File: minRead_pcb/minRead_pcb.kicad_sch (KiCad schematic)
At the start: 0 parts

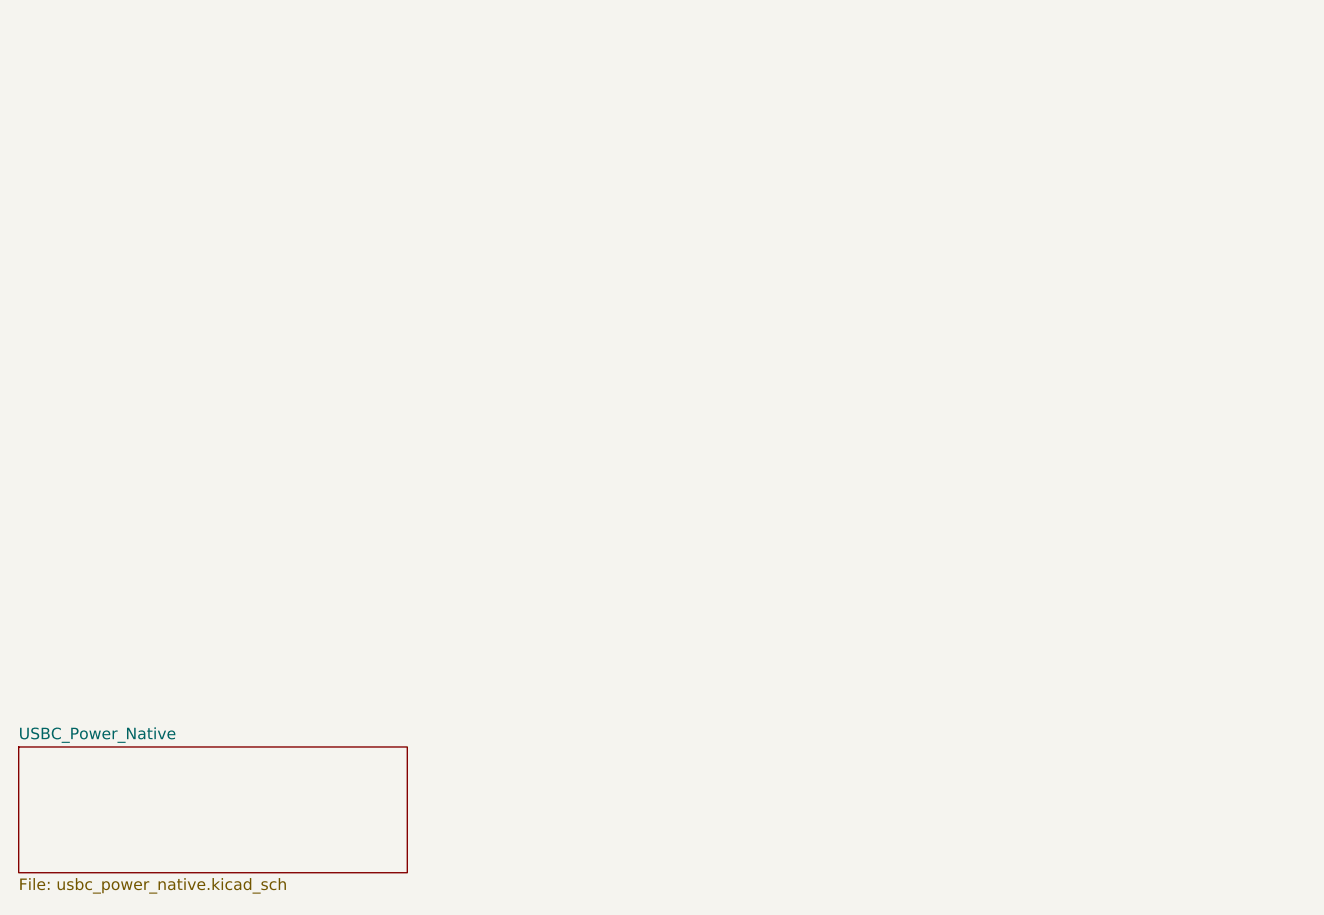
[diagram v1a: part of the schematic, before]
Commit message: - fixed diode orientation of eink booster - everything works except eink driver: - rst pin pulls high, dc doesn't toggle, etc etc. - TODO for next rev: - remove reset stabilizer and just route 3v3 to epd inductor circuit - replace esd arrays with hand-solderable components (qfn to sot) - replace buttons with resistor ladder circuit (xteink-like) - replace bq24074 with more discrete charging circuit to aid hand-solder - add led driver (15v to 7 series LEDs) - replace usb-c receptacle with through-hole - add external dupont pins for external LED driver access and spare GPIOs
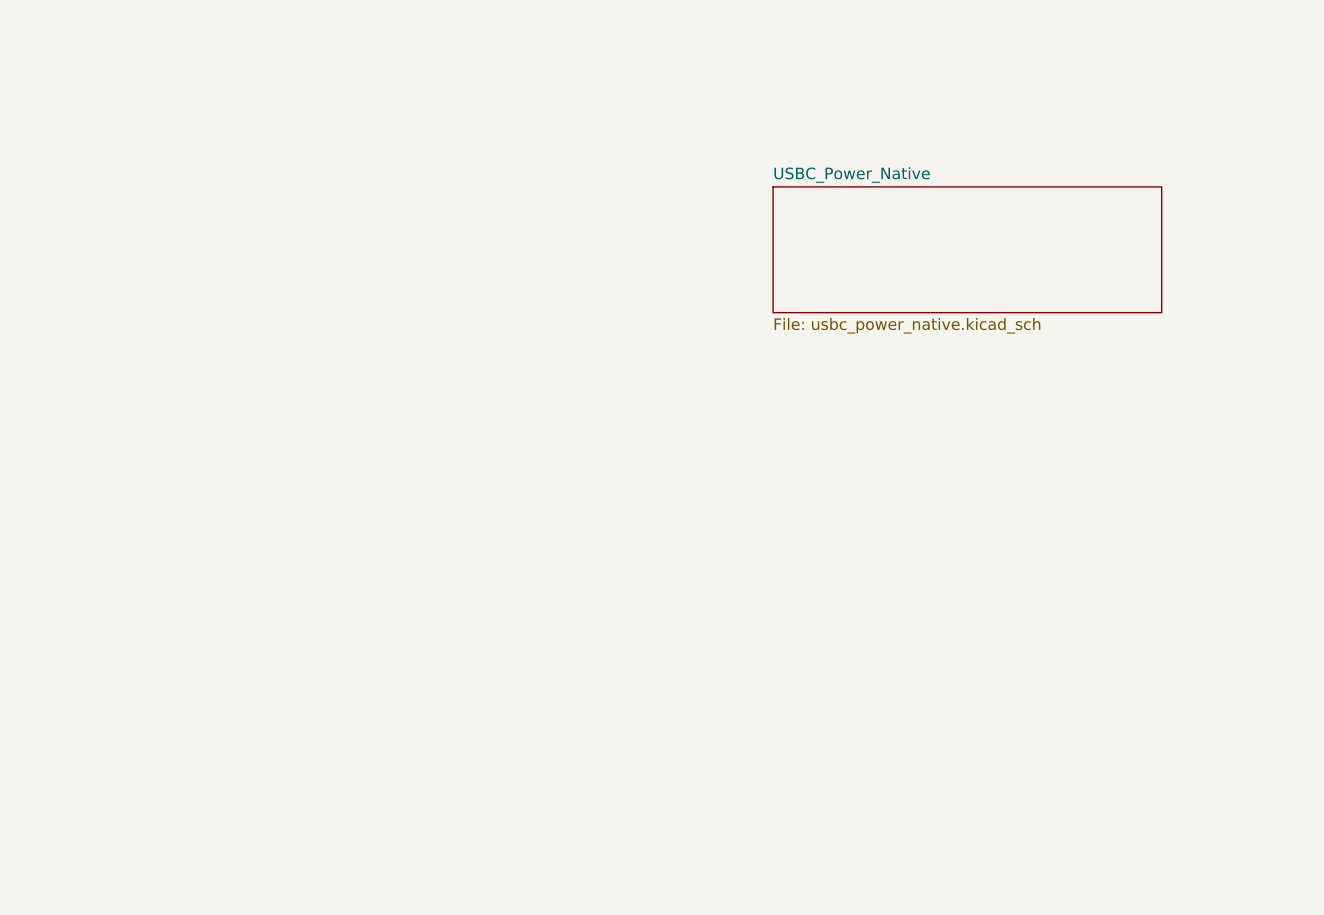
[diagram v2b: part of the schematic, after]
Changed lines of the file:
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@@
 	)
 	(sheet
-		(at 27.94 180.34)
+		(at 111.76 118.11)
 		(size 43.18 13.97)
 		(exclude_from_sim no)
@@
 		)
 		(property "Sheetname" "USBC_Power_Native"
-			(at 27.94 179.6284 0)
+			(at 111.76 117.3984 0)
 			(effects
 				(font
@@
 		)
 		(property "Sheetfile" "usbc_power_native.kicad_sch"
-			(at 27.94 194.8946 0)
+			(at 111.76 132.6646 0)
 			(effects
 				(font

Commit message: gigantic commit, my bad revised schematic to sanity check turns out my fpc was flipped, now fixed added following schematics: - battery protection circuit - series LED driver - external peripheral connector for unused GPIO revised following schematics: - power path, replaced with mcp charger and FET rather than bq - buttons, opted for resistor ladder circuit, added two more for xte compatibility - eink driver, opted to change to updated components from waveshare 2.3 - updated esd components for usb-c and sdmmc - updated usb-c receptacle, now through-hole
New layout:
- mostly same as last time, but work done to ensure good grounding for LED/eink circuits
- eink gpio has minimal crossing/coupling just in case
- esp32 and 24 pin headers have longer pads hopefully for easier soldering
- external header in corner back of device
- prettier passive component layout
- fat 3v3 traces and small zone fill

- todo:
- DRC errors, mostly clearance and silkscreen overlap
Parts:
- added C1: 1n, Capacitor_SMD:C_0805_2012Metric_Pad1.18x1.45mm_HandSolder, symbol Device:C
- added C10, C11, C12, C13, C14, C15, C16, C17, C2, C3, C37: 4.7u, Capacitor_SMD:C_0805_2012Metric_Pad1.18x1.45mm_HandSolder, symbol Device:C
- added C18, C19, C20, C22, C5, C9: 1u, Capacitor_SMD:C_0805_2012Metric_Pad1.18x1.45mm_HandSolder, symbol Device:C
- added C32, C4, C6: 22u, Capacitor_SMD:C_0805_2012Metric_Pad1.18x1.45mm_HandSolder, symbol Device:C
- added C33, C36, C7, C8: 0.1u, Capacitor_SMD:C_0805_2012Metric_Pad1.18x1.45mm_HandSolder, symbol Device:C
- added CR1: TSD05CDYFR, footprints:TVS_SOD2_DYF_TEX-M, symbol TSD05CDYFR:TSD05CDYFR
- added D1, D2, D3, D4, D5, D6: MBR0530, Diode_SMD:D_SOD-123, symbol Diode:MBR0530
- added H1, H2, H3, H4: MountingHole_Pad, MountingHole:MountingHole_2.2mm_M2_DIN965_Pad_TopBottom, symbol Mechanical:MountingHole_Pad
- added J1: USB_C_Receptacle, Connector_USB:USB_C_Receptacle_GCT_USB4085, symbol Connector:USB_C_Receptacle_USB2.0_14P
- added J2: FH34SRJ-24S-0.5SH_50_, FH34SRJ-24S-0.5SH(50):HRS_FH34SRJ-24S-0.5SH_50_, symbol FH34SRJ-24S-0.5SH(50):FH34SRJ-24S-0.5SH_50_
- added J3: FH34SRJ-6S-0.5SH_50_, FH34SRJ-6S-0.5SH(50):HRS_FH34SRJ-6S-0.5SH_50_, symbol FH34SRJ-6S-0.5SH(50):FH34SRJ-6S-0.5SH_50_
- added J4: PPTC062LFBN-RC, XPYC062LFBN-RC, symbol PPTC_12:PPTC062LFBN-RC
- added J5: Conn_01x02, Connector_JST:JST_PH_S2B-PH-K_1x02_P2.00mm_Horizontal, symbol Connector_Generic:Conn_01x02
- added J7: Micro_SD_Card, Connector_Card:microSD_HC_Hirose_DM3AT-SF-PEJM5, symbol Connector:Micro_SD_Card
- added L1, L2: 10u, srn3010C-100m:IND_SRN3010C-100M, symbol Device:L
- added Q1: FS8205A, Package_TO_SOT_SMD:SOT-23-6_Handsoldering, symbol FS8205A:FS8205A
- added Q2, Q3: IRLML6402, Package_TO_SOT_SMD:SOT-23_Handsoldering, symbol Transistor_FET:IRLML6402
- added Q4, Q5, Q6: BSS138, Package_TO_SOT_SMD:SOT-23, symbol Transistor_FET:BSS138
- added R1: 1M, Resistor_SMD:R_0805_2012Metric_Pad1.20x1.40mm_HandSolder, symbol Device:R
- added R10: 47k, Resistor_SMD:R_0805_2012Metric_Pad1.20x1.40mm_HandSolder, symbol Device:R
- added R11: 12k, Resistor_SMD:R_0805_2012Metric_Pad1.20x1.40mm_HandSolder, symbol Device:R
- added R12: 100k, Resistor_SMD:R_0805_2012Metric_Pad1.20x1.40mm_HandSolder, symbol Device:R
- added R13, R15, R28, R4, R53, R54, R55, R6, R7, R8, R9: 10k, Resistor_SMD:R_0805_2012Metric_Pad1.20x1.40mm_HandSolder, symbol Device:R
- added R14: 3, Resistor_SMD:R_0805_2012Metric_Pad1.20x1.40mm_HandSolder, symbol Device:R
- added R16: 1k, Resistor_SMD:R_0805_2012Metric_Pad1.20x1.40mm_HandSolder, symbol Device:R
- added R17: 100, Resistor_SMD:R_0805_2012Metric_Pad1.20x1.40mm_HandSolder, symbol Device:R
- added R18: 5.6k, Resistor_SMD:R_0805_2012Metric_Pad1.20x1.40mm_HandSolder, symbol Device:R
- added R19: 20k, Resistor_SMD:R_0805_2012Metric_Pad1.20x1.40mm_HandSolder, symbol Device:R
- added R2, R3: 5.1k, Resistor_SMD:R_0805_2012Metric_Pad1.20x1.40mm_HandSolder, symbol Device:R
- added R20: 56k, Resistor_SMD:R_0805_2012Metric_Pad1.20x1.40mm_HandSolder, symbol Device:R
- added R21, R22, R23, R24, R25, R26, R29, R30, R31, R32, R33, R34: 33, Resistor_SMD:R_0805_2012Metric_Pad1.20x1.40mm_HandSolder, symbol Device:R
- added R27: 0, Resistor_SMD:R_0805_2012Metric_Pad1.20x1.40mm_HandSolder, symbol Device:R
- added R35: 33k, Resistor_SMD:R_0805_2012Metric_Pad1.20x1.40mm_HandSolder, symbol Device:R
- added R36: 75k, Resistor_SMD:R_0805_2012Metric_Pad1.20x1.40mm_HandSolder, symbol Device:R
- added R37: 82, Resistor_SMD:R_0805_2012Metric_Pad1.20x1.40mm_HandSolder, symbol Device:R
- added R5: 8.9k, Resistor_SMD:R_0805_2012Metric_Pad1.20x1.40mm_HandSolder, symbol Device:R
- added SW1, SW10, SW4, SW5, SW7: SW_Push, Button_Switch_THT:SW_Tactile_SPST_Angled_PTS645Vx39-2LFS, symbol Switch:SW_Push
- added SW12, SW2, SW3, SW6, SW8, SW9: SW_Push, Button_Switch_SMD:SW_SPST_PTS810, symbol Switch:SW_Push
- added U1, U6: TPD4E1U06DBVR, Package_TO_SOT_SMD:SOT-23-6_Handsoldering, symbol TPD4E1U06DBVR:TPD4E1U06DBVR
- added U2: AP3012, Package_TO_SOT_SMD:SOT-23-5, symbol Regulator_Switching:AP3012
- added U3: AP2112K-3.3, Package_TO_SOT_SMD:SOT-23-5_HandSoldering, symbol Regulator_Linear:AP2112K-3.3
- added U4: ESP32-S3-WROOM-1, RF_Module:ESP32-S3-WROOM-1, symbol RF_Module:ESP32-S3-WROOM-1
- added U5: DW01A, Package_TO_SOT_SMD:SOT-23-6_Handsoldering, symbol Battery_Management:DW01A
- added U7: MCP73832-2-OT, Package_TO_SOT_SMD:SOT-23-5, symbol Battery_Management:MCP73832-2-OT
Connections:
- new net: R19.1, SW8.2
- new net: C18.2, J2.18
- new net: C19.2, J2.19
- new net: C13.2, J2.20
- new net: C15.2, J2.22
- new net: C20.2, J2.24
- new net: C17.2, J2.5
- new net: R21.1, U4.35 (IO42)
- new net: R23.1, U4.33 (IO40)
- new net: R16.2, U5.2 (CS)
- new net: D3.2 (A), L2.2, U2.1 (SW)
- new net: Q5.2 (S), Q6.2 (S), R37.1, U2.3 (FB)
- new net: R29.2, U4.17 (IO9)
- new net: R6.1, U7.5 (PROG)
- new net: D1.2 (A), J1.A4 (VBUS), J1.A9 (VBUS), J1.B4 (VBUS), J1.B9 (VBUS)
- new net: C1.2, J1.S1 (SHIELD), R1.2
- new net: R35.1, SW5.2
- new net: R33.2, U4.21 (IO13)
- new net: R22.1, U4.34 (IO41)
- new net: R18.1, SW3.2
- new net: C11.2, D5.2 (A), L1.1, Q4.3 (D)
- new net: R26.1, U4.25 (IO48)
- new net: R25.1, U4.32 (IO39)
- new net: Q3.3 (D), R27.2
- new net: R24.1, U4.31 (IO38)
- new net: R20.1, SW9.2
- new net: C11.1, D4.1 (K), D6.2 (A)
- new net: R36.1, SW7.2
- new net: R11.1, SW4.2
- new net: R17.2, R27.1
- new net: R32.2, U4.20 (IO12)
- new net: R34.2, U4.22 (IO14)
- new net: R30.2, U4.18 (IO10)
- new net: R31.2, U4.19 (IO11)
- new net: Q1.4, U5.1 (OD)
- new net: Q1.6, U5.3 (OC)
- new net 3V3: C10.2, C12.2, C22.2, C32.1, C33.1, C36.2, C37.2, C6.1, J2.15, J2.16, J4.12, J7.4 (VDD), L1.2, L2.1, R13.1, R28.2, R4.2, R53.2, R54.2, R55.2, R7.1, R8.2, R9.2, SW10.1, U2.5 (IN), U3.5 (VOUT), U4.2 (3V3)
- new net B+: J5.2 (Pin_2), Q3.2 (S)
- new net B-: C7.2, J5.1 (Pin_1), Q1.1, Q3.1 (G), U5.6 (GND)
- new net BAT_MONIT: C8.1, R10.1, R12.2, U4.4 (IO4)
- new net BUTTON_ADC_1: R18.2, R19.2, R20.2, R4.1, SW2.2, U4.39 (IO1)
- new net BUTTON_ADC_2: R11.2, R28.1, R35.2, R36.2, SW1.2, U4.38 (IO2)
- new net C-: J3.2, Q5.3 (D)
- new net CC1: J1.A5 (CC1), R3.1, U6.4
- new net CC2: J1.B5 (CC2), R2.1, U6.3
- new net CHG_STATUS: U4.12 (IO8), U7.1 (STAT)
- new net COOL_TOGGLE: J4.5, Q5.1 (G), U4.7 (IO7)
- new net DN: J1.A7 (D-), J1.B7 (D-), U4.13 (USB_D-), U6.1
- new net DP: J1.A6 (D+), J1.B6 (D+), U4.14 (USB_D+), U6.6
- new net EPD_BUSY: J2.9, R34.1
- new net EPD_CS: J2.12, R31.1
- new net EPD_DC: J2.11, R32.1
- new net EPD_MOSI: J2.14, R29.1
- new net EPD_RST: J2.10, R33.1
- new net EPD_SCK: J2.13, R30.1
- new net ESP32_EN: C5.1, R7.2, SW12.2, U4.3 (EN)
- new net ESP32_IO0: R13.2, SW6.2, U4.27 (IO0)
- new net GDR: J2.2, Q4.1 (G), R15.2
- new net GND: C1.1, C10.1, C12.1, C13.1, C14.1, C15.1, C16.1, C17.1, C18.1, C19.1, C2.2, C20.1, C22.1, C3.2, C32.2, C33.2, C36.1, C37.1, C4.2, C5.2, C6.2, C8.2, C9.1, CR1.2 (GND), D6.1 (K), H1.1, H2.1, H3.1, H4.1, J1.A1 (GND), J1.A12 (GND), J1.B1 (GND), J1.B12 (GND), J2.17, J2.8, J2.S1 (SHIELD), J2.S2 (SHIELD__1), J3.S1 (SHIELD), J3.S2 (SHIELD), J4.1, J7.6 (VSS), J7.9 (SHIELD), Q1.3, R1.1, R10.2, R14.1, R15.1, R16.1, R2.2, R3.2, R37.2, R5.2, R6.2, SW1.1, SW12.1, SW2.1, SW3.1, SW4.1, SW5.1, SW6.1, SW7.1, SW8.1, SW9.1, U1.2, U2.2 (GND), U3.2 (GND), U4.1 (GND), U4.40 (GND), U4.41 (GND), U6.2, U7.2 (V_{SS})
- new net LDO_IN: C4.1, D2.1 (K), Q2.2 (S), U3.1 (VIN), U3.3 (EN)
- new net LED_SW: C9.2, D3.1 (K), J3.1, J3.5
- new net P+: C3.1, C7.1, Q2.3 (D), R12.1, R17.1, U5.5 (VCC), U7.3 (V_{BAT})
- new net PREVGH: C14.2, D5.1 (K), J2.21
- new net PREVGL: C16.2, D4.2 (A), J2.23
- new net PWM_LED: J4.2, U2.4 (~{SHDN}), U4.5 (IO5)
- new net PWR_BUTTON: SW10.2, U4.15 (IO3)
- new net RESE: J2.3, Q4.2 (S), R14.2
- new net SD_CLK: J7.5 (CLK), R25.2
- new net SD_CMD: J7.3 (CMD), R23.2, R55.1
- new net SD_DAT0: J7.7 (DAT0), R24.2, R8.1, U1.4
- new net SD_DAT1: J7.8 (DAT1), R26.2, R9.1, U1.3
- new net SD_DAT2: J7.1 (DAT2), R21.2, R53.1, U1.1
- new net SD_DAT3: J7.2 (DAT3/CD), R22.2, R54.1, U1.6
- new net UNUSED_GPIO_15: J4.7, U4.8 (IO15)
- new net UNUSED_GPIO_16: J4.9, U4.9 (IO16)
- new net UNUSED_GPIO_17: J4.11, U4.10 (IO17)
- new net UNUSED_GPIO_18: J4.10, U4.11 (IO18)
- new net UNUSED_GPIO_45: J4.4, U4.26 (IO45)
- new net UNUSED_GPIO_46: J4.6, U4.16 (IO46)
- new net UNUSED_GPIO_47: J4.8, U4.24 (IO47)
- new net USB_VBUS: C2.1, CR1.1 (I/O), D1.1 (K), D2.2 (A), Q2.1 (G), R5.1, U7.4 (V_{DD})
- new net W-: J3.6, Q6.3 (D)
- new net WARM_TOGGLE: J4.3, Q6.1 (G), U4.6 (IO6)
- no-connect marks 0 -> 14
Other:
- removed sheet Buttons
- removed sheet ESP32_S3
- removed sheet E_ink_HAT
- removed sheet LiPo_In
- removed sheet MicroSD_Out_SDMMC4bit
- removed sheet USBC_Power_Native
- note added: "- +"
- note added: "3.7V LiPo Battery Connector"
- note added: "Battery Charger"
- note added: "Battery Monitor"
- note added: "Battery<->USB Power Path Switch"
- note added: "Bootloader Buttons"
- note added: "Charge Pump"
- note added: "DOWN(1) UP(1) DOWN(2) UP(2)"
- note added: "E-ink Driver & Connector"
- note added: "ESD Protection"
- note added: "ESP32 Pin-out"
- note added: "External Peripheral Connector"
- note added: "Interface Buttons"
- note added: "LDO 3.3V"
- note added: "LED Driver & Connector"
- note added: "Local Pull-ups"
- note added: "Main Socket"
- note added: "Mounting"
- note added: "Overcharge/Discharge Protection"
- note added: "Power Button"
- note added: "RIGHT LEFT CONFIRM BACK"
- note added: "Reverse polarity protection"
- note added: "SDMMC Interface"
- note added: "USB-C Connector"
- note added: "USB-C ESD Protection"
- note added: "ZIF 24-pin Connector"

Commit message: updated some things: - confirmed battery protection circuit - added pull up to EPD_RST - changed to 10 pin external IO header instead of 12 pin - reserved gpio 17 and 18 for LED_PWR and LED_SENSE - responsible for providing 3.3V to LED circuit and detecting if the circuit is closed or not (for safety) - these are pulled high with 10k so that the LED circuit does not start unless told to in software, and that LED_SENSE goes low when it detects current through LEDs (kind of, not really, but same principle) - added indicator for inductor name - made pull down on vbus stronger for less current draw while plugged in - changed battery monitor resistors to 1M/1M for less current draw, period - added some comments on schematic - layout is done, just has a couple of minor silkscreen warnings - basically all keep-outs are gone, btw. we like to live dangerously - I think that's it?
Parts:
- removed D3: MBR0530, Diode_SMD:D_SOD-123, symbol Diode:MBR0530
- removed J4: PPTC062LFBN-RC, XPYC062LFBN-RC, symbol PPTC_12:PPTC062LFBN-RC
- added D7: MBR0540, Diode_SMD:D_SOD-123, symbol Diode:MBR0540
- added J6: PPTC052LFBN-RC, PPTC_10:CONN_PPTC052LFBN-RC_SUL, symbol PPTC_10:PPTC052LFBN-RC
- added Q7, Q8: IRLML6402, Package_TO_SOT_SMD:SOT-23_Handsoldering, symbol Transistor_FET:IRLML6402
- added Q9: MMBT3904, Package_TO_SOT_SMD:SOT-23_Handsoldering, symbol Transistor_BJT:MMBT3904
- added R38: 100k, Resistor_SMD:R_0805_2012Metric_Pad1.20x1.40mm_HandSolder, symbol Device:R
- added R39, R40, R41: 10k, Resistor_SMD:R_0805_2012Metric_Pad1.20x1.40mm_HandSolder, symbol Device:R
- added TP1, TP3, TP5, TP7: TestPoint, TestPoint:TestPoint_THTPad_1.0x1.0mm_Drill0.5mm, symbol Connector:TestPoint
- R10: value 47k -> 1M
- R12: value 100k -> 1M
- R36: value 75k -> 68k
- R5: value 8.9k -> 10k
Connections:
- net 3V3: now also R5.2, J6.10, Q7.2 (S), R40.2, R41.1; no longer C12.2, L2.1, U2.5 (IN)
- net BUTTON_ADC_1: now also TP1.1
- net C-: now also J6.2
- net EPD_RST: now also R5.1
- net GND: now also J6.1, Q8.1 (G), Q9.2 (E), R38.2; no longer R5.2
- net LED_SW: now also D7.1 (K), J6.6
- net UNUSED_GPIO_15: now also J6.4
- net UNUSED_GPIO_16: now also J6.5
- net UNUSED_GPIO_45: now also J6.3
- net UNUSED_GPIO_46: now also J6.8
- net UNUSED_GPIO_47: now also J6.9
- net USB_VBUS: now also R38.1; no longer R5.1
- net W-: now also J6.7
- net CONFIRM: now reaches R19.1, SW8.2
- net CONFIRM: now also TP5.1
- net at L2.2, U2.1 (SW): now also D7.2 (A)
- net at Q5.2 (S), Q6.2 (S), R37.1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: now also R39.2
- net LEFT: now reaches R18.1, SW3.2
- net LEFT: now also TP3.1
- net BACK: now reaches R20.1, SW9.2
- net BACK: now also TP7.1
- net at R17.2: now also Q8.2 (S); no longer R27.1
- net at Q1.4: now also U5.3 (OC); no longer U5.1 (OD)
- net at Q1.6: now also U5.1 (OD); no longer U5.3 (OC)
- net UNUSED_GPIO_17 renamed LED_PWR
- net LED_PWR: now also Q7.1 (G), R40.1
- net UNUSED_GPIO_18 renamed LED_SENSE
- net LED_SENSE: now also Q9.3 (C), R41.2
- new net: C12.2, L2.1, Q7.3 (D), U2.5 (IN)
- new net: Q8.3 (D), R27.1
- new net: Q9.1 (B), R39.1
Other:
- note added: "10kohm -> 100mA charge rate"
- note added: "3.3V min -> 1.65V"
- note added: "4.2V max -> 2.1V"
- note added: "50V"
- note added: "Explanation for Mosfet:"
- note added: "External Buttons"
- note added: "High resistor values -> low idle current"
- note added: "SRN3010C-100m"
- note added: "Taken from"
- note added: "https://tinyurl.com/4bm2ynx9"
- note added: "https://tinyurl.com/yzwe4dtf"
- note added: "pull-up on RST recommended to avoid epd wakes when in deep sleep"
- note added: "ratio will be 0.5"
- moved on the sheet: C12, C9, H1, H2, H3, H4, J3, L2, Q5, Q6, R27, R37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
